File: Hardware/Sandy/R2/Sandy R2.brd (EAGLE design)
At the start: 25.7 x 24.6 mm, 18 parts, among them SW1 RST, SW2 FLASH

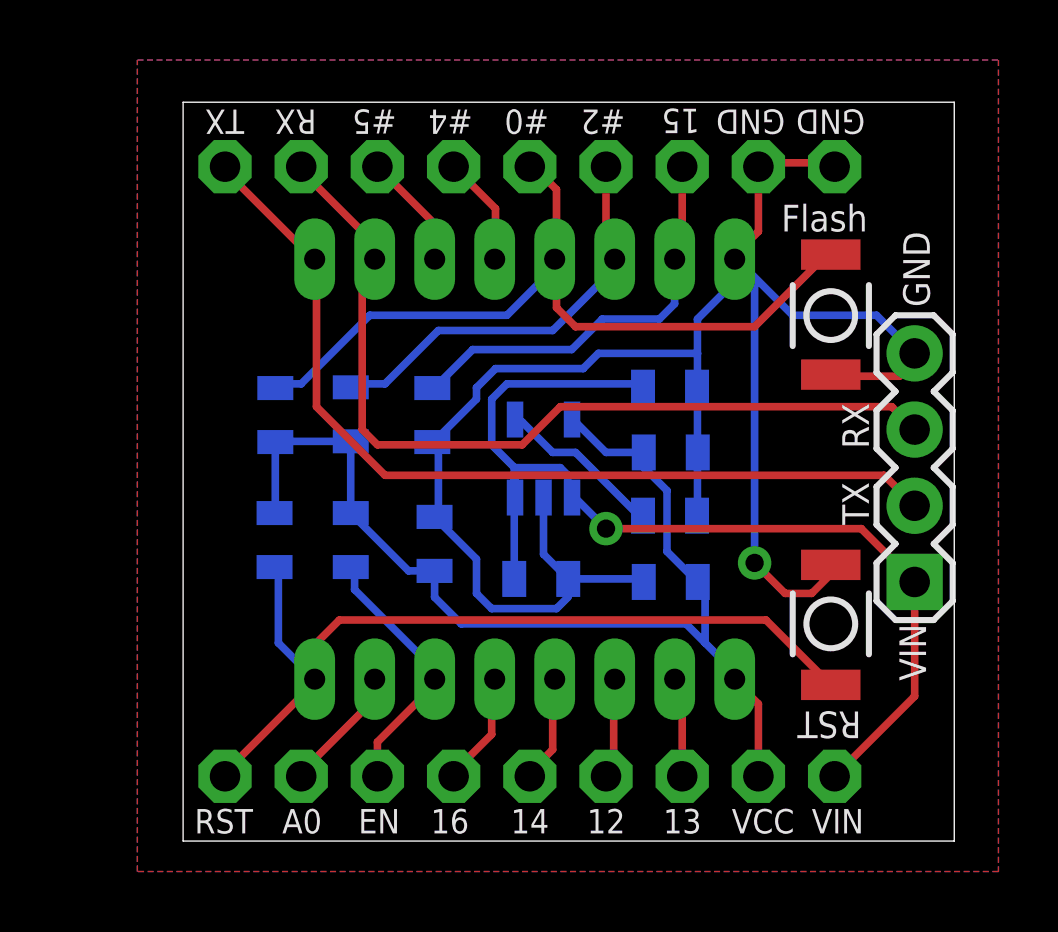
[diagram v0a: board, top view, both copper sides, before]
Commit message: Update Sandy R2: + Remove unused resistors and caps + Move 2 buttons to near side to better usability
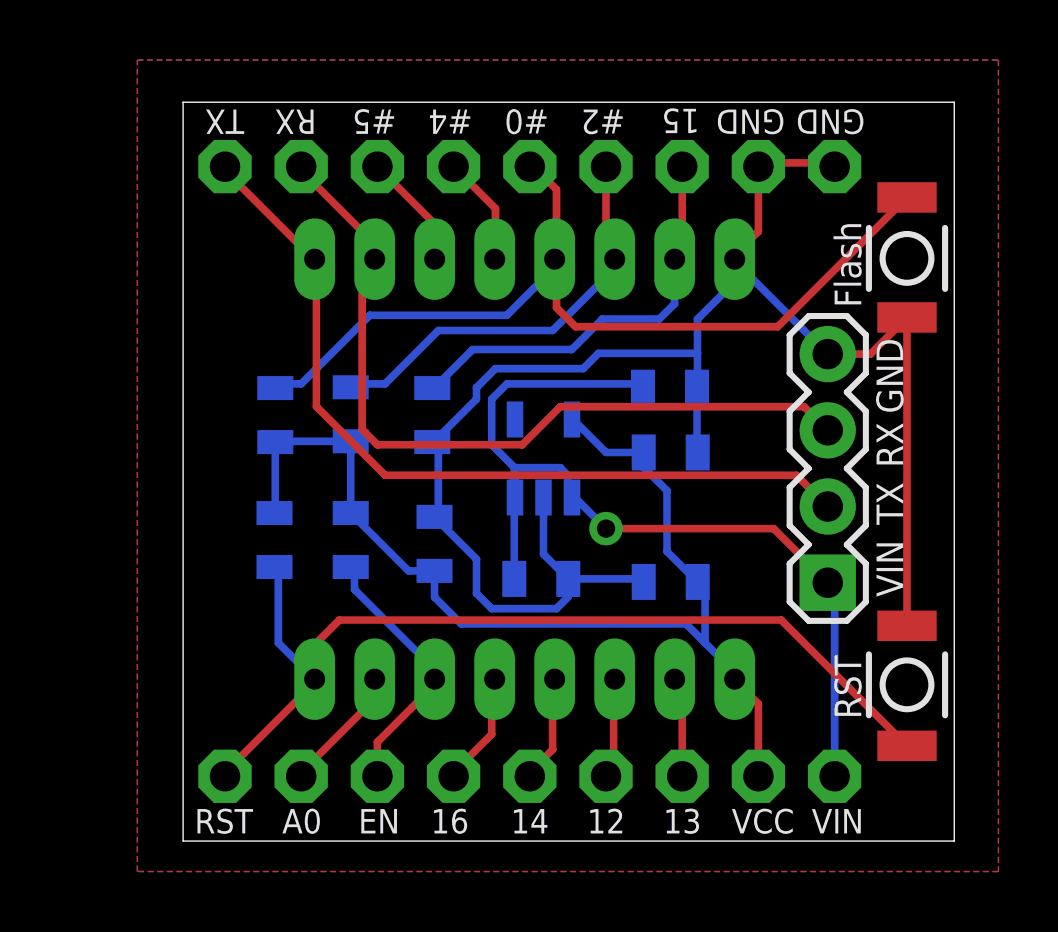
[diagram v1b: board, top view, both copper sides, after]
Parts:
- removed C3: 22nF, SparkFun-Passives:0805
- moved SW1 3.25 mm to (31.4, 16.4)
- moved SW2 3.18 mm to (31.4, 34.7)
- moved FTDI 2.90 mm to (28.7, 21.8)
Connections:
- removed net BP: C3.1, RT9013.4
- net GND: no longer C3.2
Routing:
- net GND: track 65.7 -> 57.0 mm, vias 1 -> 0
- net BP: track 5.56 -> 0.00 mm
- net VIN: track 35.1 -> 31.1 mm
- net RST: track 28.4 -> 31.8 mm
- net D3: track 27.1 -> 30.4 mm
- net TX: track 30.6 -> 27.7 mm
- net RX: track 29.4 -> 26.6 mm

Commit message: Update Sandy to move 2 switch buttons near rear side
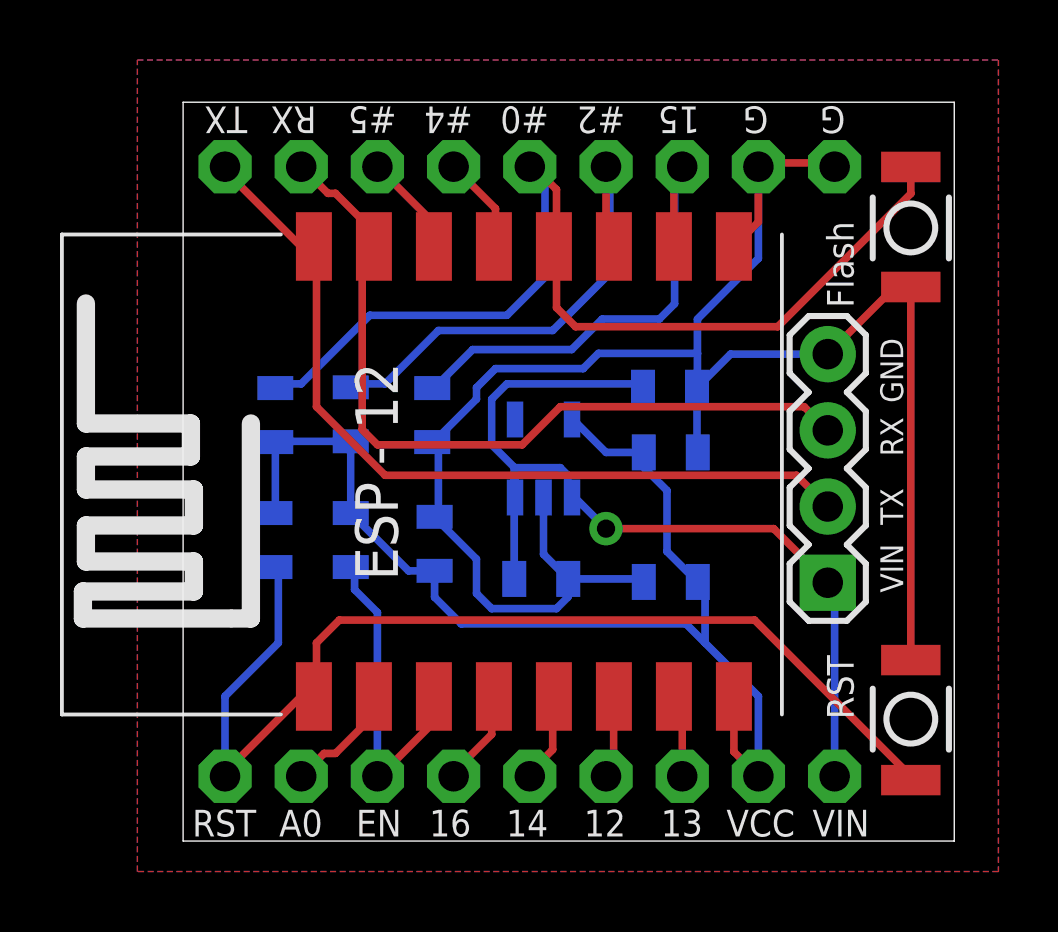
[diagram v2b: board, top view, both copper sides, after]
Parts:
- removed U2: (no value), esp8266modules:ESP12
- added U$1: ESP-12-SMD-THIN, My Eagle Lib:ESP-12-SMD-THIN
- moved SW1 1.15 mm to (31.5, 15.2)
- moved SW2 1.02 mm to (31.5, 35.7)
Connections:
- net A0: now also U$1.ADC; no longer U2.ADC
- net D0: now also U$1.GPIO16; no longer U2.GPIO16
- net D1: now also U$1.GPIO5; no longer U2.GPIO5
- net D2: now also U$1.GPIO4; no longer U2.GPIO4
- net D3: now also U$1.GPIO0; no longer U2.GPIO0
- net D4: now also U$1.GPIO2; no longer U2.GPIO2
- net D5: now also U$1.GPIO14; no longer U2.GPIO14
- net D6: now also U$1.GPIO12; no longer U2.GPIO12
- net D7: now also U$1.GPIO13; no longer U2.GPIO13
- net D8: now also U$1.GPIO15; no longer U2.GPIO15
- net EN: now also U$1.CH_PD; no longer U2.CH_PD
- net GND: now also U$1.GND; no longer U2.GND
- net RST: now also U$1.RESET; no longer U2.RESET
- net RX: now also U$1.RXD0; no longer U2.RX
- net TX: now also U$1.TXD0; no longer U2.TX
- net VCC: now also U$1.VCC; no longer U2.VCC
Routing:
- net GND: track 57.0 -> 62.9 mm
- net RST: track 31.8 -> 36.1 mm
- net D3: track 30.4 -> 34.3 mm
- net VCC: track 36.8 -> 39.8 mm
- net D8: track 14.0 -> 16.7 mm
- net D4: track 14.2 -> 16.8 mm
- net EN: track 9.12 -> 10.8 mm
- net D7: track 3.43 -> 2.77 mm
- net D0: track 3.82 -> 3.19 mm
- net D5: track 3.58 -> 2.98 mm
- net D6: track 3.35 -> 2.77 mm
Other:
- board text added: "G"
